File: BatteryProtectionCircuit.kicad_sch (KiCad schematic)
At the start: 44 parts, among them J1 Conn_01x04_Pin, J2 Conn_01x07_Pin, J3 Conn_01x03_Pin, J4 Conn_01x04_Pin, Q1 NMOS, U2 LM358, U3 LM358, U4 LM321, U6 LMC555xN

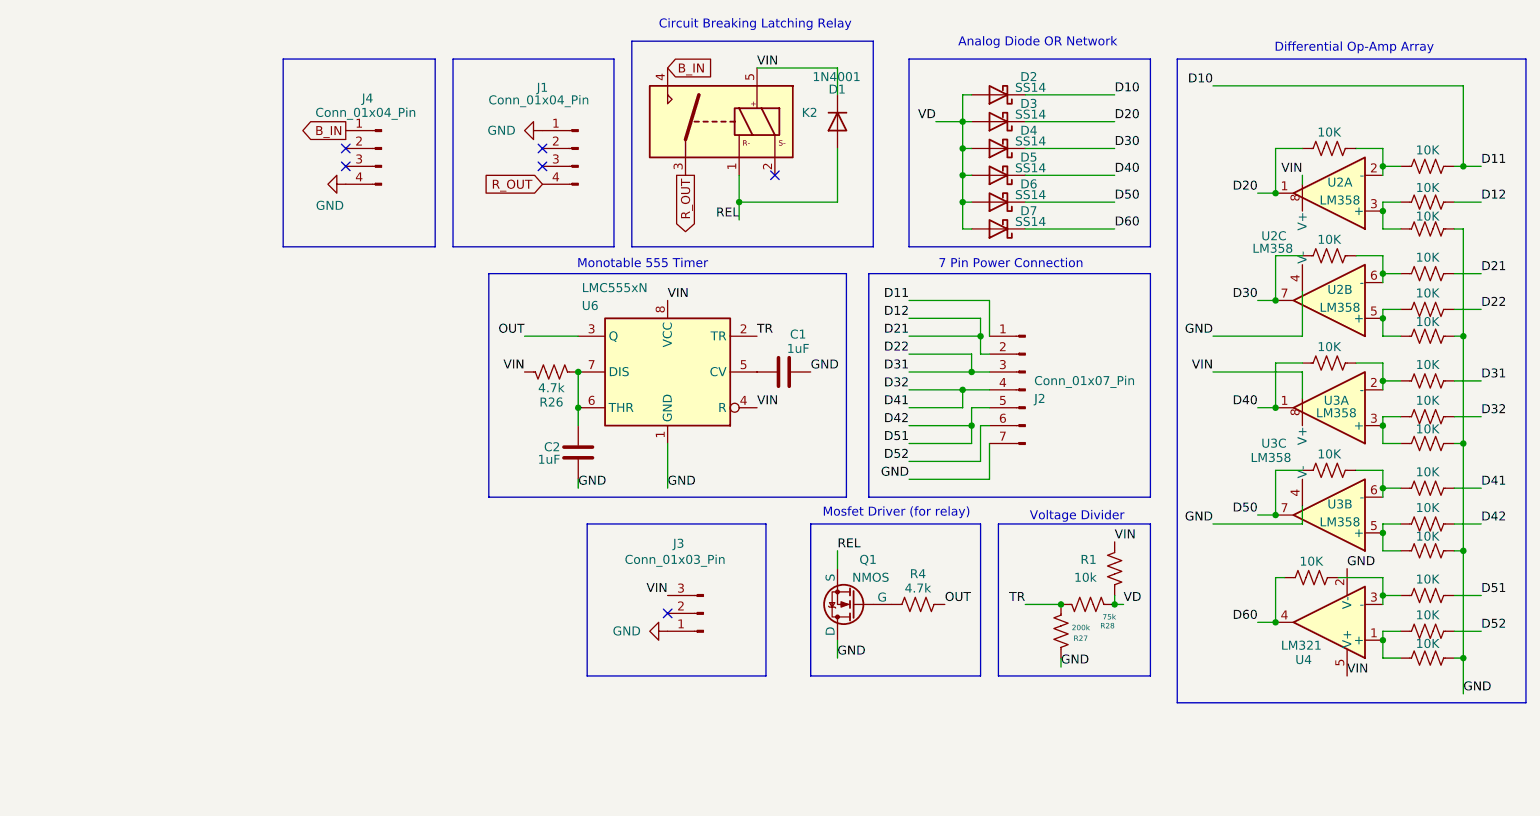
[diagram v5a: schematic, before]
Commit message: Finalized(?) PCB tracing
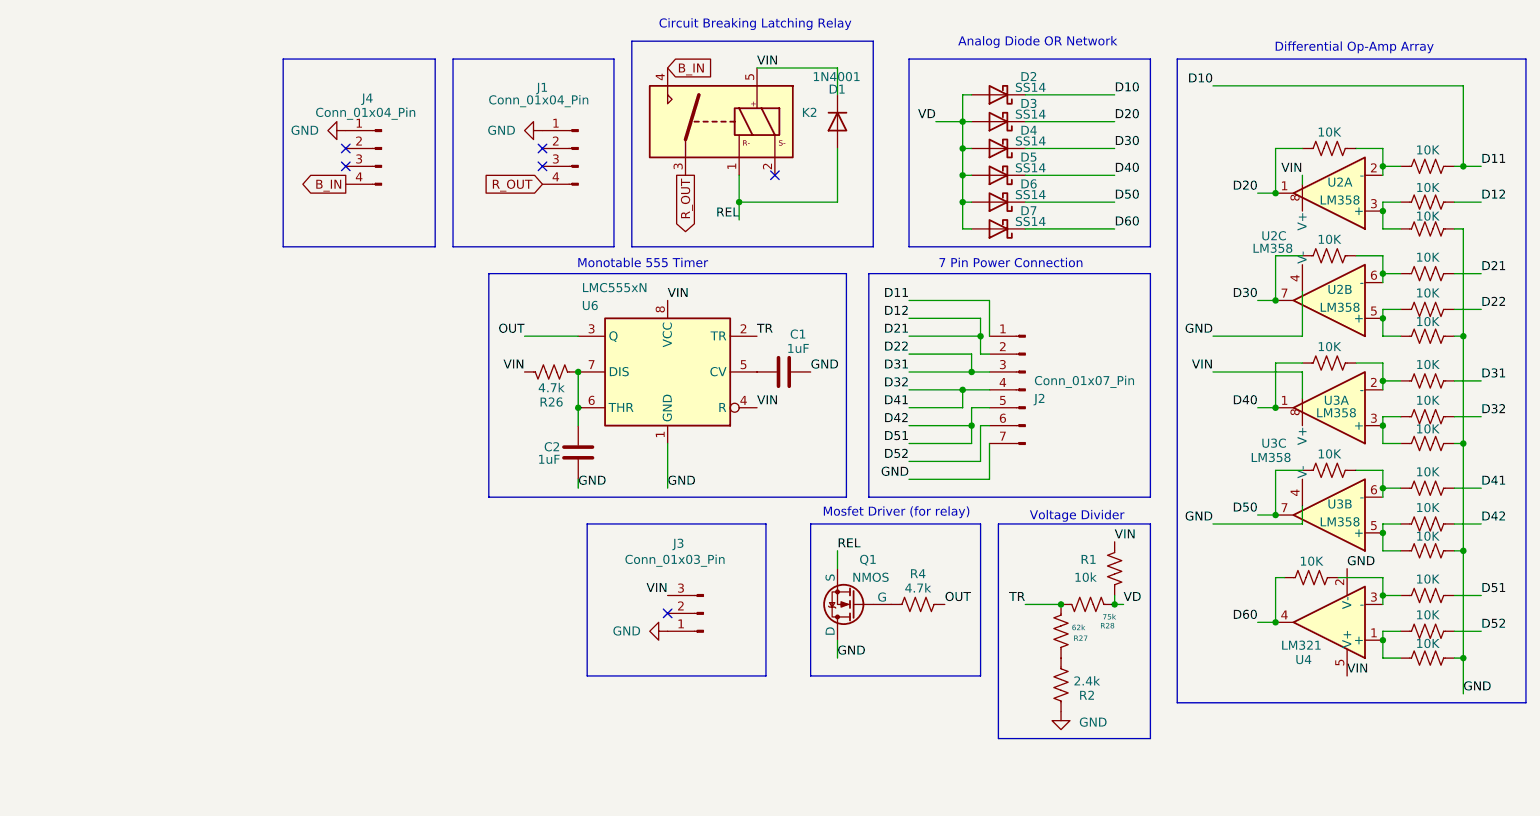
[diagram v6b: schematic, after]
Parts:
- added R2: 2.4k, Resistor_SMD:R_0805_2012Metric, symbol Device:R_US
- R27: value 200k -> 62k
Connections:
- net B_IN: now also J4.4 (Pin_4); no longer J4.1 (Pin_1)
- net GND: now also J4.1 (Pin_1), R2.2; no longer J4.4 (Pin_4), R27.1
- new net: R2.1, R27.1
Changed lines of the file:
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@@
 	(rectangle
 		(start 185.42 95.25)
-		(end 207.01 116.84)
+		(end 207.01 125.73)
 		(stroke
 			(width 0)
@@
 	(wire
 		(pts
-			(xy 194.31 114.3) (xy 194.31 115.57)
-		)
-		(stroke
-			(width 0)
-			(type default)
-		)
-	)
-	(wire
-		(pts
 			(xy 240.03 74.93) (xy 240.03 72.39)
 		)
@@
 		)
 	)
-	(label "GND"
-		(at 194.31 115.57 0)
-		(effects
-			(font
-				(size 1.27 1.27)
-			)
-			(justify left bottom)
-		)
-	)
 	(label "OUT"
 		(at 177.8 106.68 0)
@@
 	(global_label "B_IN"
 		(shape output)
-		(at 92.71 39.37 180)
+		(at 92.71 46.99 180)
 		(fields_autoplaced yes)
 		(effects
@@
 		)
 		(property "Intersheetrefs" "${INTERSHEET_REFS}"
-			(at 85.5519 39.37 0)
+			(at 85.5519 46.99 0)
 			(effects
 				(font
@@
 			)
 		)
-		(property "Value" "200k"
+		(property "Value" "62k"
 			(at 195.834 109.982 0)
 			(effects
@@
 	)
 	(symbol
+		(lib_id "Device:R_US")
+		(at 194.31 118.11 0)
+		(unit 1)
+		(exclude_from_sim no)
+		(in_bom yes)
+		(on_board yes)
+		(dnp no)
+		(property "Reference" "R2"
+			(at 196.85 119.634 0)
+			(effects
+				(font
+					(size 1.27 1.27)
+				)
+				(justify left)
+			)
+		)
+		(property "Value" "2.4k"
+			(at 196.088 117.602 0)
+			(effects
+				(font
+					(size 1.27 1.27)
+				)
+				(justify left)
+			)
+		)
+		(property "Footprint" "Resistor_SMD:R_0805_2012Metric"
+			(at 195.326 118.364 90)
+			(effects
+				(font
+					(size 1.27 1.27)
+				)
+				(hide yes)
+			)
+		)
+		(property "Datasheet" "~"
+			(at 194.31 118.11 0)
+			(effects
+				(font
+					(size 1.27 1.27)
+				)
+				(hide yes)
+			)
+		)
+		(property "Description" "Resistor, US symbol"
+			(at 194.31 118.11 0)
+			(effects
+				(font
+					(size 1.27 1.27)
+				)
+				(hide yes)
+			)
+		)
+		(pin "2"
+		)
+		(pin "1"
+		)
+		(instances
+			(project ""
+				(path "/299dddd9-ac06-42a6-950e-710b9bcf8f9e"
+					(reference "R2")
+					(unit 1)
+				)
+			)
+		)
+	)
+	(symbol
 		(lib_id "Amplifier_Operational:LM358")
 		(at 232.41 93.98 180)
@@
 	)
 	(symbol
+		(lib_id "power:GND")
+		(at 92.71 39.37 270)
+		(unit 1)
+		(exclude_from_sim no)
+		(in_bom yes)
+		(on_board yes)
+		(dnp no)
+		(fields_autoplaced yes)
+		(property "Reference" "#PWR01"
+			(at 86.36 39.37 0)
+			(effects
+				(font
+					(size 1.27 1.27)
+				)
+				(hide yes)
+			)
+		)
+		(property "Value" "GND"
+			(at 88.9 39.3699 90)
+			(effects
+				(font
+					(size 1.27 1.27)
+				)
+				(justify right)
+			)
+		)
+		(property "Footprint" ""
+			(at 92.71 39.37 0)
+			(effects
+				(font
+					(size 1.27 1.27)
+				)
+				(hide yes)
+			)
+		)
+		(property "Datasheet" ""
+			(at 92.71 39.37 0)
+			(effects
+				(font
+					(size 1.27 1.27)
+				)
+				(hide yes)
+			)
+		)
+		(property "Description" "Power symbol creates a global label with name \"GND\" , ground"
+			(at 92.71 39.37 0)
+			(effects
+				(font
+					(size 1.27 1.27)
+				)
+				(hide yes)
+			)
+		)
+		(pin "1"
+		)
+		(instances
+			(project ""
+				(path "/299dddd9-ac06-42a6-950e-710b9bcf8f9e"
+					(reference "#PWR01")
+					(unit 1)
+				)
+			)
+		)
+	)
+	(symbol
 		(lib_id "Device:R_US")
 		(at 246.38 53.34 90)
@@
 	(symbol
 		(lib_id "power:GND")
+		(at 194.31 121.92 0)
+		(unit 1)
+		(exclude_from_sim no)
+		(in_bom yes)
+		(on_board yes)
+		(dnp no)
+		(property "Reference" "#PWR04"
+			(at 194.31 128.27 0)
+			(effects
+				(font
+					(size 1.27 1.27)
+				)
+				(hide yes)
+			)
+		)
+		(property "Value" "GND"
+			(at 198.882 123.444 0)
+			(effects
+				(font
+					(size 1.27 1.27)
+				)
+			)
+		)
+		(property "Footprint" ""
+			(at 194.31 121.92 0)
+			(effects
+				(font
+					(size 1.27 1.27)
+				)
+				(hide yes)
+			)
+		)
+		(property "Datasheet" ""
+			(at 194.31 121.92 0)
+			(effects
+				(font
+					(size 1.27 1.27)
+				)
+				(hide yes)
+			)
+		)
+		(property "Description" "Power symbol creates a global label with name \"GND\" , ground"
+			(at 194.31 121.92 0)
+			(effects
+				(font
+					(size 1.27 1.27)
+				)
+				(hide yes)
+			)
+		)
+		(pin "1"
+		)
+		(instances
+			(project ""
+				(path "/299dddd9-ac06-42a6-950e-710b9bcf8f9e"
+					(reference "#PWR04")
+					(unit 1)
+				)
+			)
+		)
+	)
+	(symbol
+		(lib_id "power:GND")
 		(at 120.65 39.37 270)
 		(unit 1)
@@
 					(unit 1)
 				)
-			)
-		)
-	)
-	(symbol
-		(lib_id "power:GND")
-		(at 92.71 46.99 270)
-		(unit 1)
-		(exclude_from_sim no)
-		(in_bom yes)
-		(on_board yes)
-		(dnp no)
-		(property "Reference" "#PWR01"
-			(at 86.36 46.99 0)
-			(effects
-				(font
-					(size 1.27 1.27)
-				)
-				(hide yes)
-			)
-		)
-		(property "Value" "GND"
-			(at 92.456 50.038 90)
-			(effects
-				(font
-					(size 1.27 1.27)
-				)
-				(justify right)
-			)
-		)
-		(property "Footprint" ""
-			(at 92.71 46.99 0)
-			(effects
-				(font
-					(size 1.27 1.27)
-				)
-				(hide yes)
-			)
-		)
-		(property "Datasheet" ""
-			(at 92.71 46.99 0)
-			(effects
-				(font
-					(size 1.27 1.27)
-				)
-				(hide yes)
-			)
-		)
-		(property "Description" "Power symbol creates a global label with name \"GND\" , ground"
-			(at 92.71 46.99 0)
-			(effects
-				(font
-					(size 1.27 1.27)
-				)
-				(hide yes)
-			)
-		)
-		(pin "1"
-		)
-		(instances
-			(project "BatteryProtectionCircuit"
-				(path "/299dddd9-ac06-42a6-950e-710b9bcf8f9e"
-					(reference "#PWR01")
-					(unit 1)
-				)

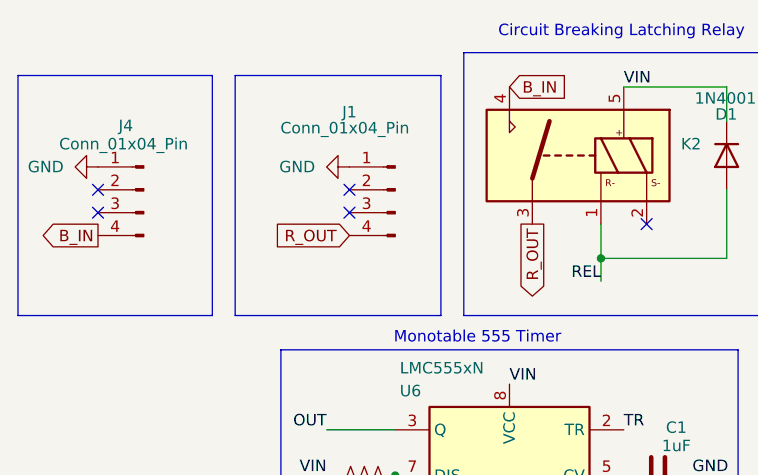
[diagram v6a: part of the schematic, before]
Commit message: Updated Trace Widths
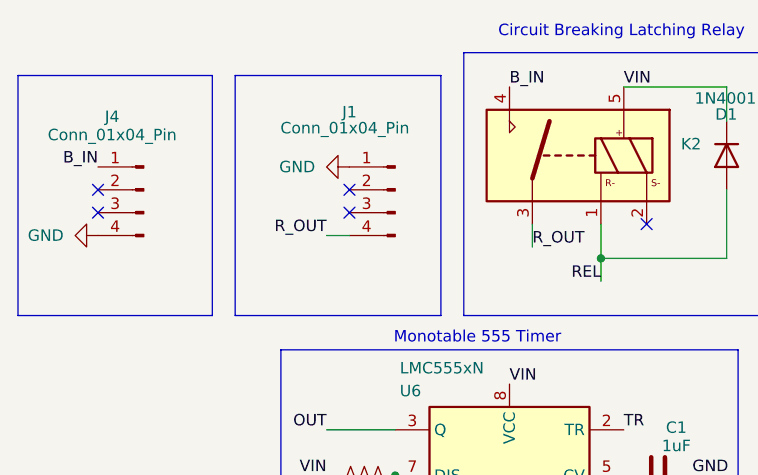
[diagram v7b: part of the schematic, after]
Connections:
- net B_IN: now also J4.1 (Pin_1); no longer J4.4 (Pin_4)
- net GND: now also J4.4 (Pin_4); no longer J4.1 (Pin_1)
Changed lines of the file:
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@@
 	(wire
 		(pts
+			(xy 118.11 46.99) (xy 120.65 46.99)
+		)
+		(stroke
+			(width 0)
+			(type default)
+		)
+	)
+	(wire
+		(pts
 			(xy 222.25 48.26) (xy 224.79 48.26)
 		)
@@
 	(wire
 		(pts
+			(xy 140.97 48.26) (xy 140.97 45.72)
+		)
+		(stroke
+			(width 0)
+			(type default)
+		)
+	)
+	(wire
+		(pts
 			(xy 138.43 83.82) (xy 138.43 90.17)
 		)
@@
 		)
 	)
+	(label "B_IN"
+		(at 92.71 39.37 180)
+		(effects
+			(font
+				(size 1.27 1.27)
+			)
+			(justify right bottom)
+		)
+	)
 	(label "D21"
 		(at 254 59.69 0)
@@
 		)
 	)
+	(label "B_IN"
+		(at 138.43 30.48 0)
+		(effects
+			(font
+				(size 1.27 1.27)
+			)
+			(justify left bottom)
+		)
+	)
 	(label "D10"
 		(at 215.9 33.02 180)
@@
 		)
 	)
+	(label "R_OUT"
+		(at 118.11 46.99 180)
+		(effects
+			(font
+				(size 1.27 1.27)
+			)
+			(justify right bottom)
+		)
+	)
 	(label "D60"
 		(at 222.25 109.22 180)
@@
 		)
 	)
+	(label "R_OUT"
+		(at 140.97 48.26 0)
+		(effects
+			(font
+				(size 1.27 1.27)
+			)
+			(justify left bottom)
+		)
+	)
 	(label "VD"
 		(at 203.2 106.68 0)
@@
 		)
 	)
-	(global_label "B_IN"
-		(shape output)
-		(at 92.71 46.99 180)
-		(fields_autoplaced yes)
-		(effects
-			(font
-				(size 1.27 1.27)
-			)
-			(justify right)
-		)
-		(property "Intersheetrefs" "${INTERSHEET_REFS}"
-			(at 85.5519 46.99 0)
-			(effects
-				(font
-					(size 1.27 1.27)
-				)
-				(justify right)
-				(hide yes)
-			)
-		)
-	)
-	(global_label "R_OUT"
-		(shape output)
-		(at 140.97 45.72 270)
-		(fields_autoplaced yes)
-		(effects
-			(font
-				(size 1.27 1.27)
-			)
-			(justify right)
-		)
-		(property "Intersheetrefs" "${INTERSHEET_REFS}"
-			(at 140.97 54.5714 90)
-			(effects
-				(font
-					(size 1.27 1.27)
-				)
-				(justify right)
-				(hide yes)
-			)
-		)
-	)
-	(global_label "R_OUT"
-		(shape input)
-		(at 120.65 46.99 180)
-		(fields_autoplaced yes)
-		(effects
-			(font
-				(size 1.27 1.27)
-			)
-			(justify right)
-		)
-		(property "Intersheetrefs" "${INTERSHEET_REFS}"
-			(at 111.7986 46.99 0)
-			(effects
-				(font
-					(size 1.27 1.27)
-				)
-				(justify right)
-				(hide yes)
-			)
-		)
-	)
-	(global_label "B_IN"
-		(shape input)
-		(at 138.43 30.48 0)
-		(fields_autoplaced yes)
-		(effects
-			(font
-				(size 1.27 1.27)
-			)
-			(justify left)
-		)
-		(property "Intersheetrefs" "${INTERSHEET_REFS}"
-			(at 145.5881 30.48 0)
-			(effects
-				(font
-					(size 1.27 1.27)
-				)
-				(justify left)
-				(hide yes)
-			)
-		)
-	)
 	(symbol
 		(lib_id "power:GND")
@@
 	)
 	(symbol
-		(lib_id "power:GND")
-		(at 92.71 39.37 270)
-		(unit 1)
-		(exclude_from_sim no)
-		(in_bom yes)
-		(on_board yes)
-		(dnp no)
-		(fields_autoplaced yes)
-		(property "Reference" "#PWR01"
-			(at 86.36 39.37 0)
-			(effects
-				(font
-					(size 1.27 1.27)
-				)
-				(hide yes)
-			)
-		)
-		(property "Value" "GND"
-			(at 88.9 39.3699 90)
-			(effects
-				(font
-					(size 1.27 1.27)
-				)
-				(justify right)
-			)
-		)
-		(property "Footprint" ""
-			(at 92.71 39.37 0)
-			(effects
-				(font
-					(size 1.27 1.27)
-				)
-				(hide yes)
-			)
-		)
-		(property "Datasheet" ""
-			(at 92.71 39.37 0)
-			(effects
-				(font
-					(size 1.27 1.27)
-				)
-				(hide yes)
-			)
-		)
-		(property "Description" "Power symbol creates a global label with name \"GND\" , ground"
-			(at 92.71 39.37 0)
-			(effects
-				(font
-					(size 1.27 1.27)
-				)
-				(hide yes)
-			)
-		)
-		(pin "1"
-		)
-		(instances
-			(project ""
-				(path "/299dddd9-ac06-42a6-950e-710b9bcf8f9e"
-					(reference "#PWR01")
-					(unit 1)
-				)
-			)
-		)
-	)
-	(symbol
 		(lib_id "Device:R_US")
 		(at 246.38 53.34 90)
@@
 		(dnp no)
 		(property "Reference" "J4"
-			(at 94.996 34.798 0)
+			(at 93.472 33.782 0)
 			(effects
 				(font
@@
 		)
 		(property "Value" "Conn_01x04_Pin"
-			(at 88.392 36.83 0)
+			(at 87.122 35.814 0)
 			(effects
 				(font
@@
 					(unit 1)
 				)
+			)
+		)
+	)
+	(symbol
+		(lib_id "power:GND")
+		(at 92.71 46.99 270)
+		(unit 1)
+		(exclude_from_sim no)
+		(in_bom yes)
+		(on_board yes)
+		(dnp no)
+		(fields_autoplaced yes)
+		(property "Reference" "#PWR01"
+			(at 86.36 46.99 0)
+			(effects
+				(font
+					(size 1.27 1.27)
+				)
+				(hide yes)
+			)
+		)
+		(property "Value" "GND"
+			(at 88.9 46.9899 90)
+			(effects
+				(font
+					(size 1.27 1.27)
+				)
+				(justify right)
+			)
+		)
+		(property "Footprint" ""
+			(at 92.71 46.99 0)
+			(effects
+				(font
+					(size 1.27 1.27)
+				)
+				(hide yes)
+			)
+		)
+		(property "Datasheet" ""
+			(at 92.71 46.99 0)
+			(effects
+				(font
+					(size 1.27 1.27)
+				)
+				(hide yes)
+			)
+		)
+		(property "Description" "Power symbol creates a global label with name \"GND\" , ground"
+			(at 92.71 46.99 0)
+			(effects
+				(font
+					(size 1.27 1.27)
+				)
+				(hide yes)
+			)
+		)
+		(pin "1"
+		)
+		(instances
+			(project ""
+				(path "/299dddd9-ac06-42a6-950e-710b9bcf8f9e"
+					(reference "#PWR01")
+					(unit 1)
+				)
